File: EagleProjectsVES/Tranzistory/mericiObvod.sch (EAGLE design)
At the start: 107 parts, among them IC1 TLC272D, IC2 TLC272D, IC3 NE555D, IC4 NE555D, IC5 TLC271D, K1 M3XXH, K2 M3XXH, K3 M3XXH, K4 M3XXH, Q1 BD140, T1 BC547, T2 BC547, T3 BC557B, U12V SMKDSP_1,5/2

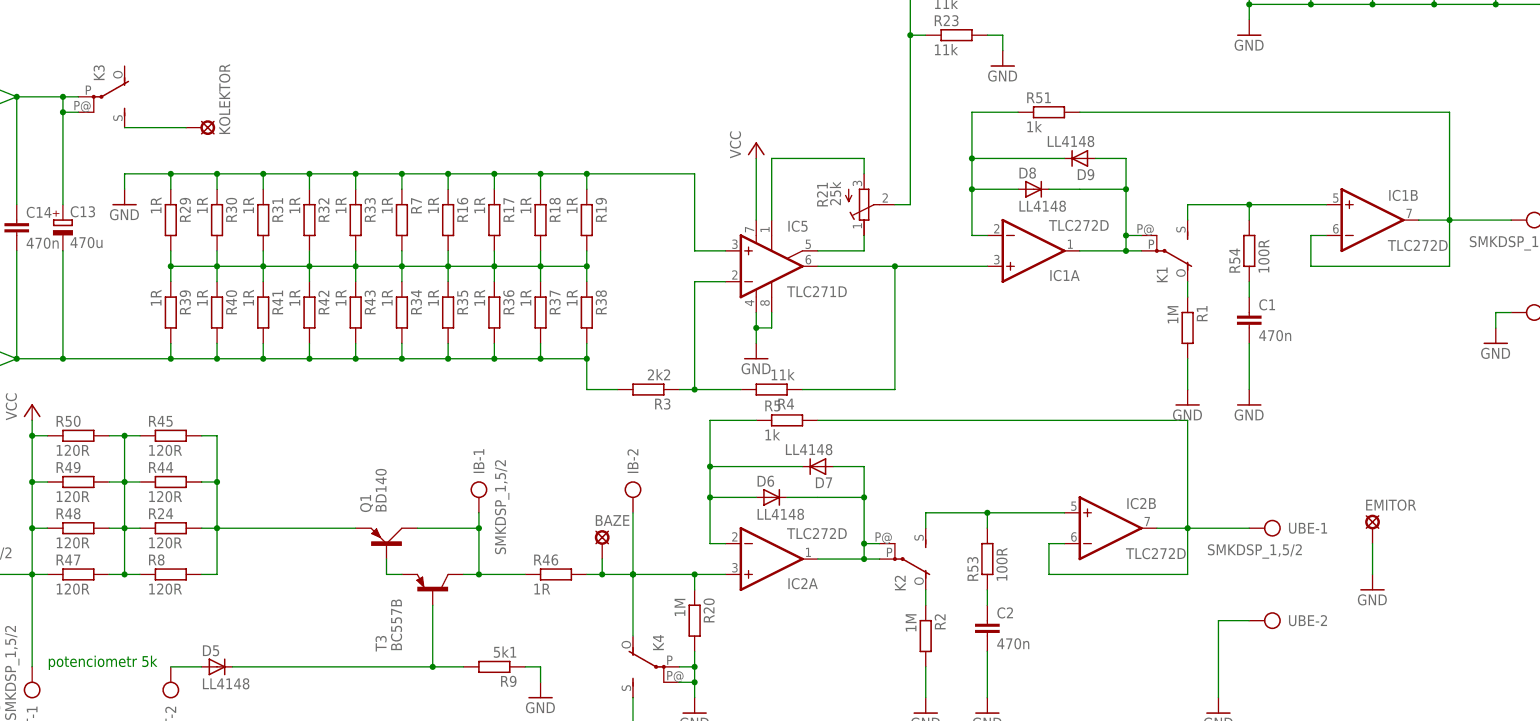
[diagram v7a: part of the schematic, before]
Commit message: Tranzistory: - opravena dalsi chybka v napojeni emitoru a serioveho rezistoru
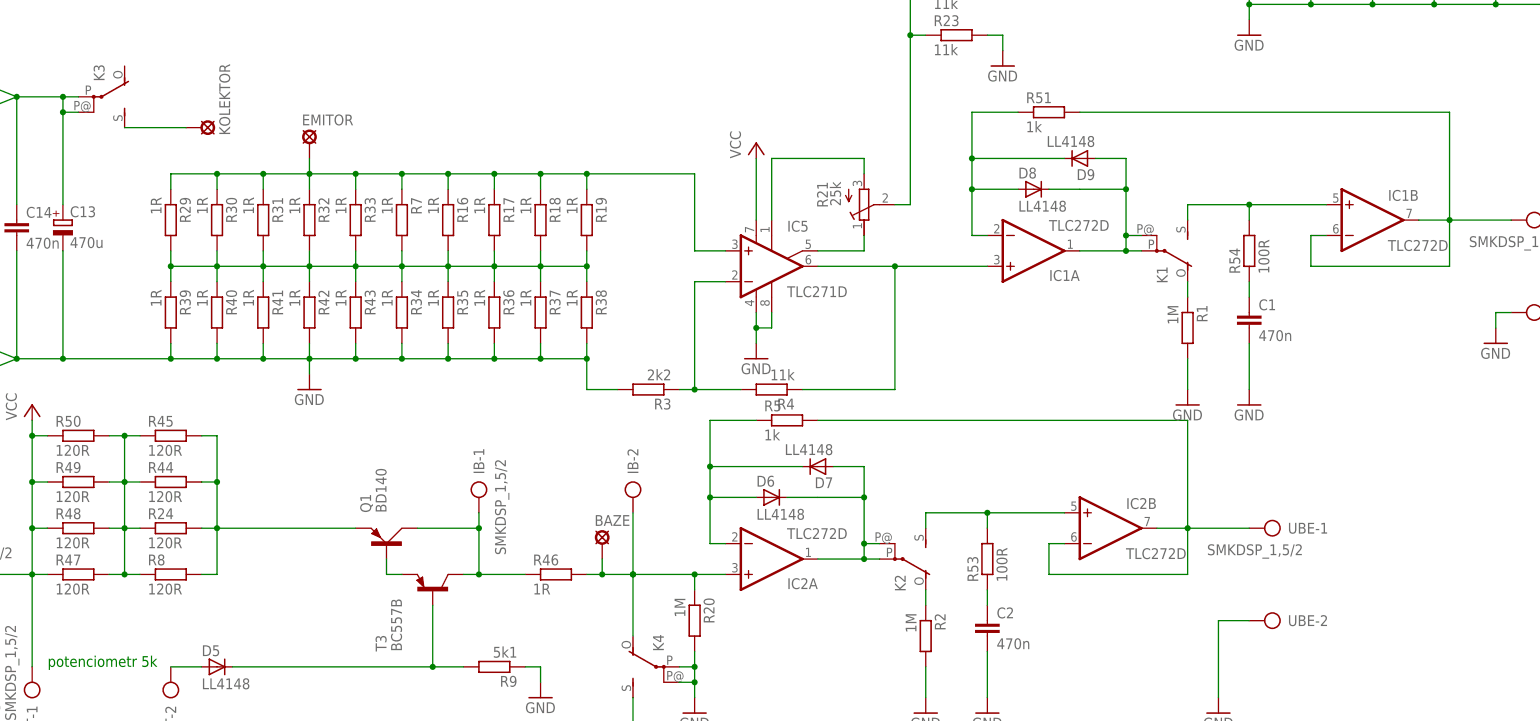
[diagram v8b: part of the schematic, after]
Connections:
- removed net N$48: C13.-, C14.2, R3.2, R34.2, R35.2, R36.2, R37.2, R38.2, R39.2, R40.2, R41.2, R42.2, R43.2, UCE1-2.KL, UCE2-2.KL
- new net N$43: EMITOR.MP, IC5.+IN, R16.1, R17.1, R18.1, R19.1, R29.1, R30.1, R31.1, R32.1, R33.1, R7.1
- net GND: now also C13.-, C14.2, R3.2, R34.2, R35.2, R36.2, R37.2, R38.2, R39.2, R40.2, R41.2, R42.2, R43.2, UCE1-2.KL, UCE2-2.KL; no longer EMITOR.MP, IC5.+IN, R16.1, R17.1, R18.1, R19.1, R29.1, R30.1, R31.1, R32.1, R33.1, R7.1
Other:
- moved on the sheet: EMITOR
